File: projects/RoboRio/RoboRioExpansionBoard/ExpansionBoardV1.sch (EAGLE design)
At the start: 36 parts, among them IC1 MCP3008, Q1 5MHz

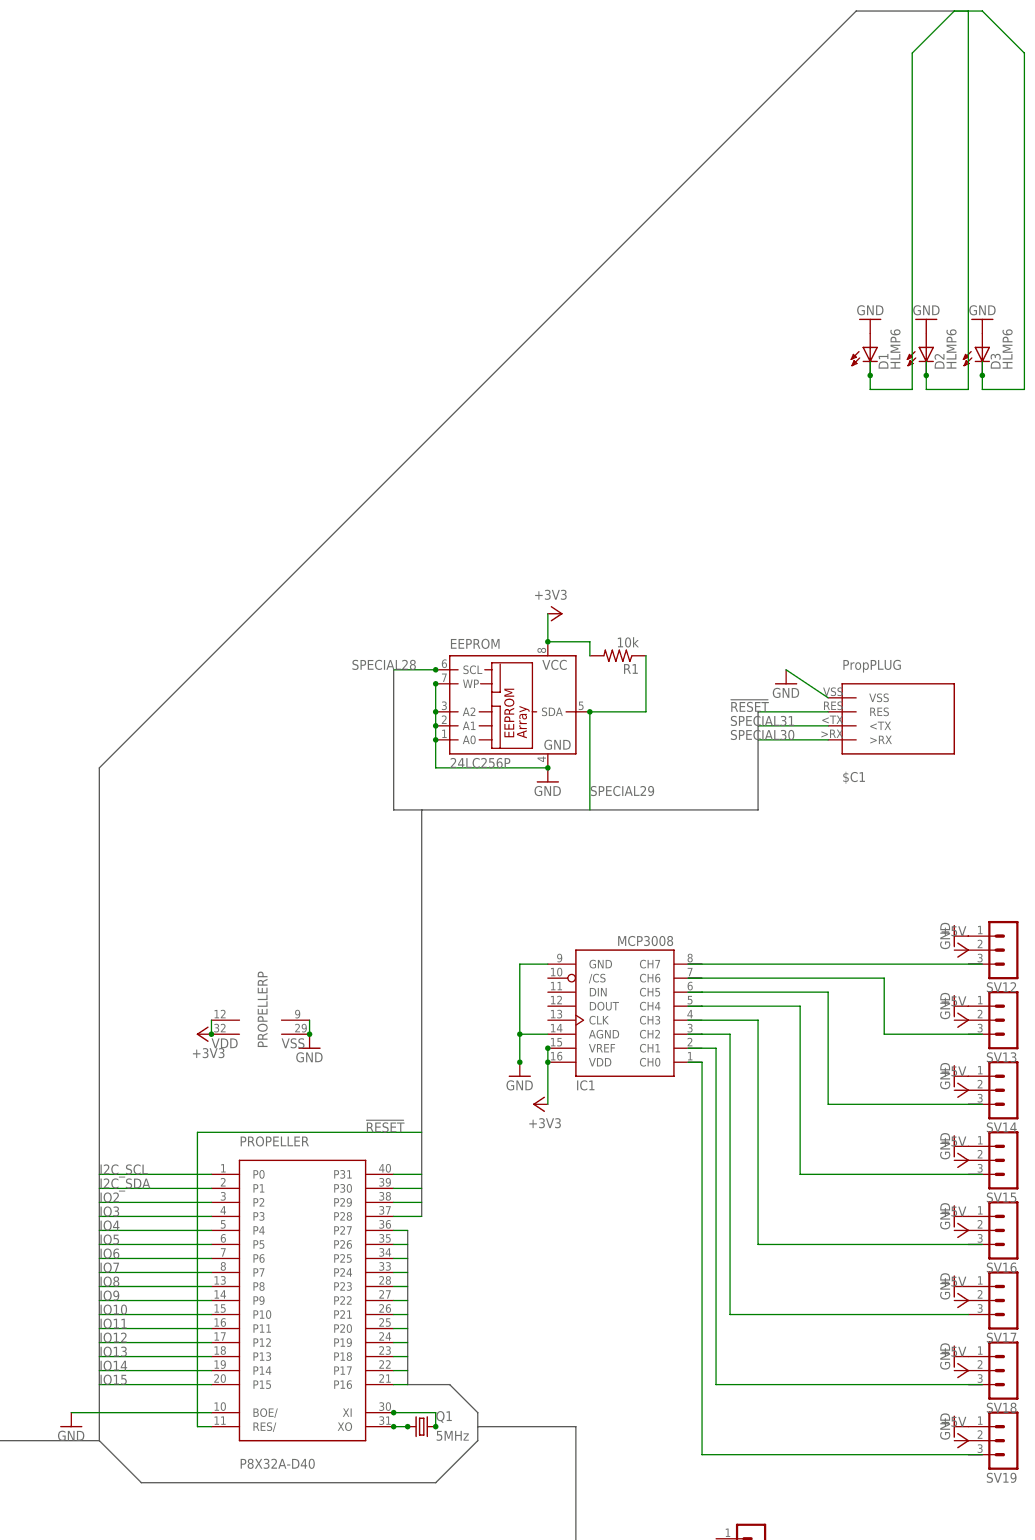
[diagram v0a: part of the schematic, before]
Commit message: RE-Revised LED location
And made them take up significantly less space.
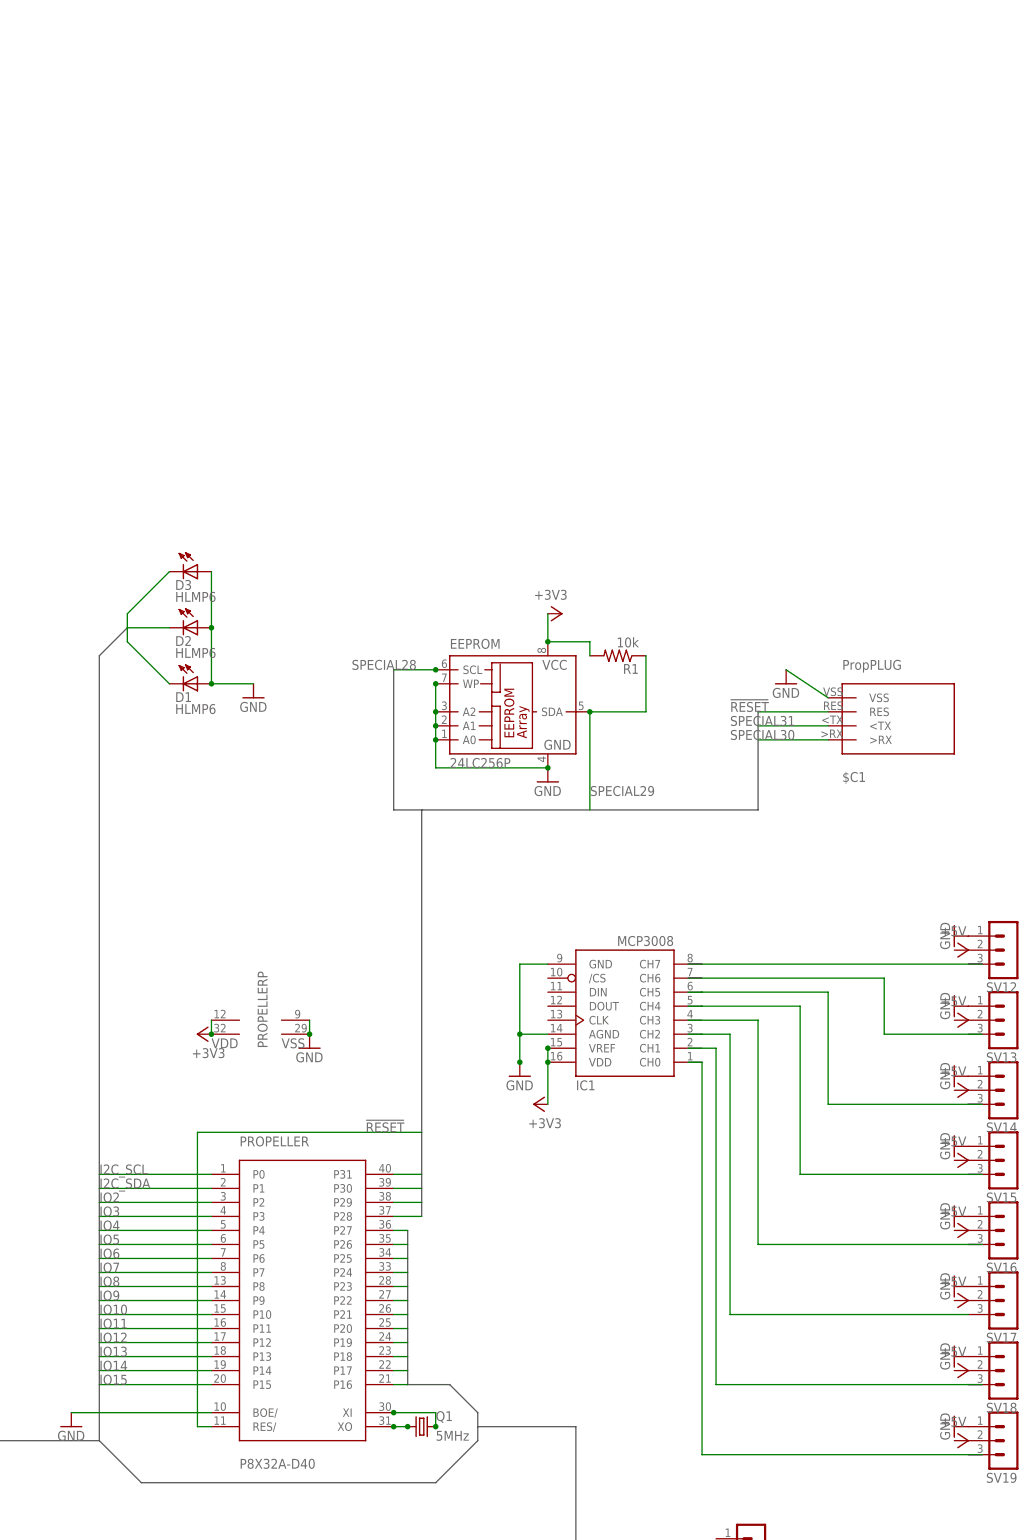
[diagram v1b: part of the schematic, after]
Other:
- moved on the sheet: D1, D2, D3
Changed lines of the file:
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@@
 <part name="D2" library="display-hp" deviceset="HLMP6" device=""/>
 <part name="D3" library="display-hp" deviceset="HLMP6" device=""/>
-<part name="GND8" library="supply1" deviceset="GND" device=""/>
-<part name="GND9" library="supply1" deviceset="GND" device=""/>
 <part name="GND10" library="supply1" deviceset="GND" device=""/>
 <part name="SV12" library="con-lstb" deviceset="MA03-1" device=""/>
@@
 <instance part="GND7" gate="1" x="78.74" y="114.3"/>
 <instance part="+3V5" gate="G$1" x="81.28" y="109.22" rot="R90"/>
-<instance part="D1" gate="A" x="142.24" y="243.84"/>
-<instance part="D2" gate="A" x="152.4" y="243.84"/>
-<instance part="D3" gate="A" x="162.56" y="243.84"/>
-<instance part="GND8" gate="1" x="142.24" y="251.46" rot="R180"/>
-<instance part="GND9" gate="1" x="152.4" y="251.46" rot="R180"/>
-<instance part="GND10" gate="1" x="162.56" y="251.46" rot="R180"/>
+<instance part="D1" gate="A" x="17.78" y="185.42" rot="R270"/>
+<instance part="D2" gate="A" x="17.78" y="195.58" rot="R270"/>
+<instance part="D3" gate="A" x="17.78" y="205.74" rot="R270"/>
+<instance part="GND10" gate="1" x="30.48" y="182.88"/>
 <instance part="SV12" gate="G$1" x="167.64" y="137.16" rot="R180"/>
 <instance part="SV13" gate="G$1" x="167.64" y="124.46" rot="R180"/>
@@
 <wire x1="10.16" y1="40.64" x2="2.54" y2="48.26" width="0.762" layer="92"/>
 <wire x1="2.54" y1="48.26" x2="-63.5" y2="48.26" width="0.762" layer="92"/>
-<wire x1="2.54" y1="48.26" x2="2.54" y2="170.18" width="0.762" layer="92"/>
-<wire x1="2.54" y1="170.18" x2="139.7" y2="307.34" width="0.762" layer="92"/>
-<wire x1="139.7" y1="307.34" x2="160.02" y2="307.34" width="0.762" layer="92"/>
+<wire x1="2.54" y1="48.26" x2="2.54" y2="190.5" width="0.762" layer="92"/>
+<wire x1="2.54" y1="190.5" x2="7.62" y2="195.58" width="0.762" layer="92"/>
 <wire x1="71.12" y1="50.8" x2="88.9" y2="50.8" width="0.762" layer="92"/>
 <wire x1="88.9" y1="50.8" x2="88.9" y2="-50.8" width="0.762" layer="92"/>
@@
 <segment>
 <pinref part="D1" gate="A" pin="A"/>
-<pinref part="GND8" gate="1" pin="GND"/>
-</segment>
-<segment>
+<pinref part="GND10" gate="1" pin="GND"/>
+<wire x1="30.48" y1="185.42" x2="22.86" y2="185.42" width="0.1524" layer="91"/>
+<pinref part="D3" gate="A" pin="A"/>
 <pinref part="D2" gate="A" pin="A"/>
-<pinref part="GND9" gate="1" pin="GND"/>
-</segment>
-<segment>
-<pinref part="D3" gate="A" pin="A"/>
-<pinref part="GND10" gate="1" pin="GND"/>
+<wire x1="22.86" y1="195.58" x2="22.86" y2="205.74" width="0.1524" layer="91"/>
+<wire x1="22.86" y1="195.58" x2="22.86" y2="185.42" width="0.1524" layer="91"/>
+<junction x="22.86" y="185.42"/>
+<junction x="22.86" y="195.58"/>
 </segment>
 <segment>
@@
 </segment>
 <segment>
-<wire x1="162.56" y1="238.76" x2="162.56" y2="241.3" width="0.1524" layer="91"/>
-<wire x1="162.56" y1="241.3" x2="162.56" y2="243.84" width="0.1524" layer="91"/>
-<wire x1="170.18" y1="238.76" x2="162.56" y2="238.76" width="0.1524" layer="91"/>
-<wire x1="170.18" y1="299.72" x2="170.18" y2="238.76" width="0.1524" layer="91"/>
-<wire x1="160.02" y1="307.34" x2="162.56" y2="307.34" width="0.1524" layer="91"/>
-<wire x1="162.56" y1="307.34" x2="170.18" y2="299.72" width="0.1524" layer="91"/>
+<wire x1="7.62" y1="195.58" x2="7.62" y2="198.12" width="0.1524" layer="91"/>
+<wire x1="7.62" y1="198.12" x2="15.24" y2="205.74" width="0.1524" layer="91"/>
 <pinref part="D3" gate="A" pin="K"/>
-<junction x="162.56" y="241.3"/>
 </segment>
 </net>
@@
 </segment>
 <segment>
-<wire x1="160.02" y1="307.34" x2="160.02" y2="238.76" width="0.1524" layer="91"/>
-<wire x1="160.02" y1="238.76" x2="152.4" y2="238.76" width="0.1524" layer="91"/>
-<wire x1="152.4" y1="243.84" x2="152.4" y2="241.3" width="0.1524" layer="91"/>
+<wire x1="7.62" y1="195.58" x2="15.24" y2="195.58" width="0.1524" layer="91"/>
 <pinref part="D2" gate="A" pin="K"/>
-<wire x1="152.4" y1="241.3" x2="152.4" y2="238.76" width="0.1524" layer="91"/>
-<junction x="152.4" y="241.3"/>
 </segment>
 </net>
@@
 </segment>
 <segment>
-<wire x1="149.86" y1="299.72" x2="149.86" y2="238.76" width="0.1524" layer="91"/>
-<wire x1="149.86" y1="299.72" x2="157.48" y2="307.34" width="0.1524" layer="91"/>
-<wire x1="160.02" y1="307.34" x2="157.48" y2="307.34" width="0.1524" layer="91"/>
-<wire x1="142.24" y1="238.76" x2="142.24" y2="241.3" width="0.1524" layer="91"/>
-<wire x1="142.24" y1="241.3" x2="142.24" y2="243.84" width="0.1524" layer="91"/>
-<wire x1="149.86" y1="238.76" x2="142.24" y2="238.76" width="0.1524" layer="91"/>
+<wire x1="15.24" y1="185.42" x2="7.62" y2="193.04" width="0.1524" layer="91"/>
+<wire x1="7.62" y1="195.58" x2="7.62" y2="193.04" width="0.1524" layer="91"/>
 <pinref part="D1" gate="A" pin="K"/>
-<junction x="142.24" y="241.3"/>
-</segment>
-</net>
+</segment>
+</net>

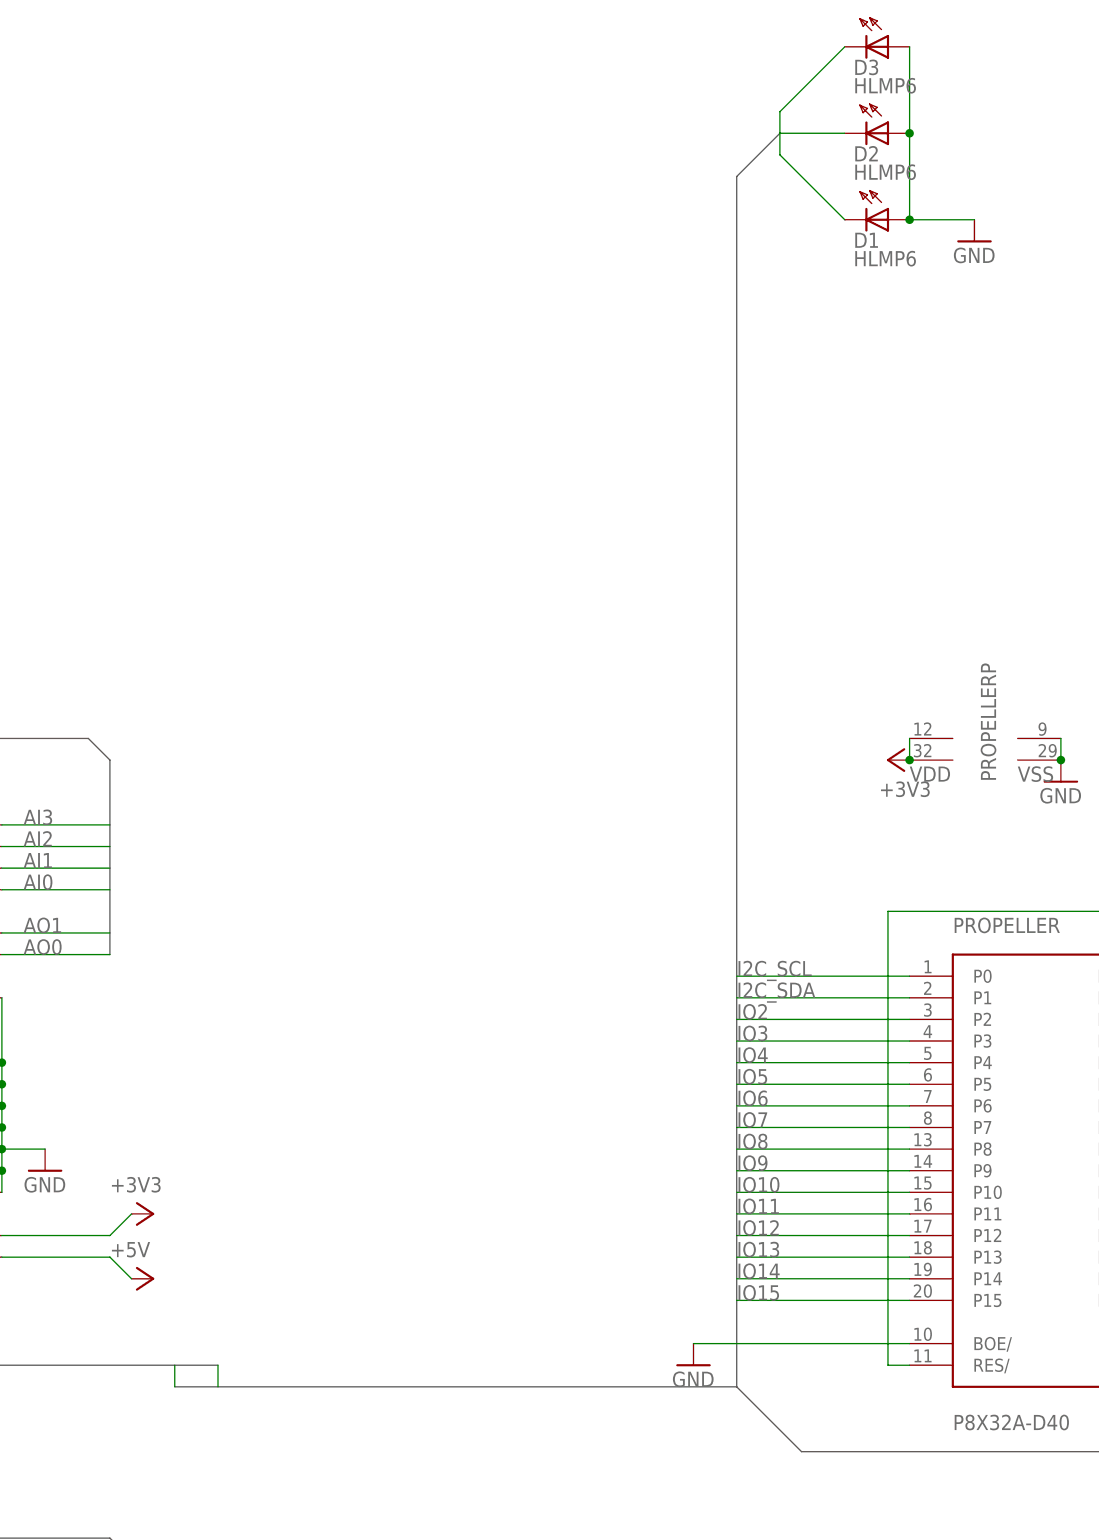
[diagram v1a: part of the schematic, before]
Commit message: Switched to SPI for the connection, adjusted LEDs
LEDs are now on pins 4..6, and named according to color
SPI is for the RoboRIO connection
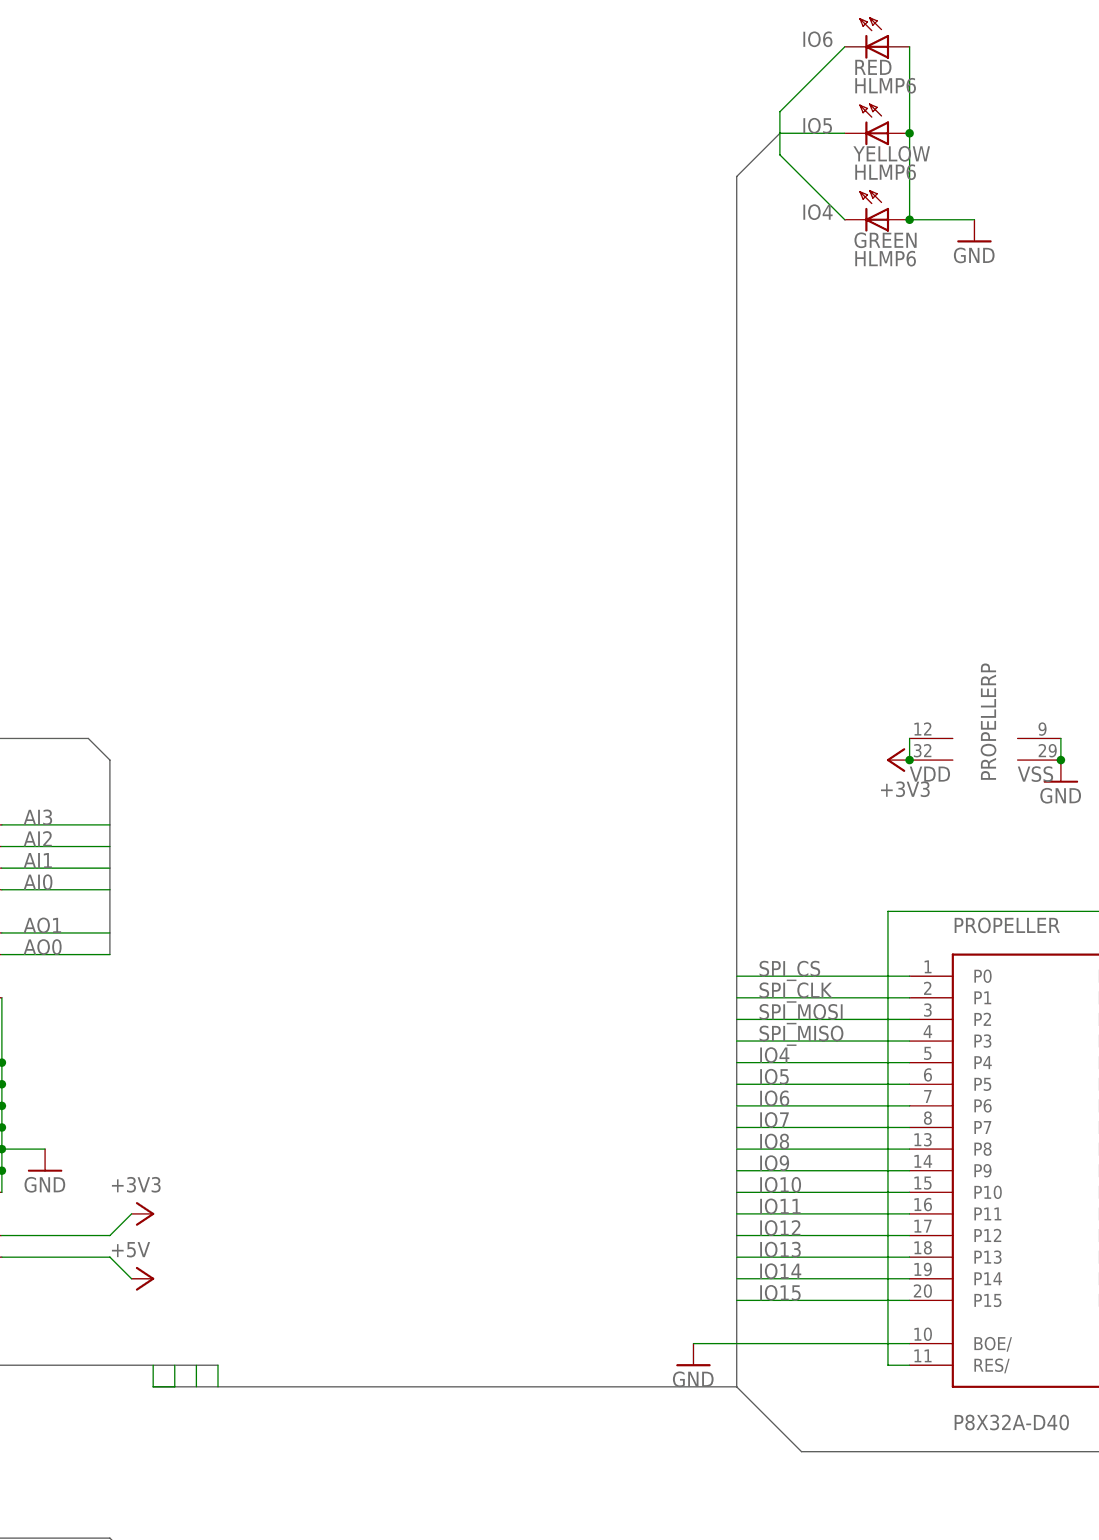
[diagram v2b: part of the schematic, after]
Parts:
- renumbered D1 to GREEN, D2 to YELLOW, D3 to RED
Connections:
- removed net IO2: PROPELLERP8X32A-D40.P2, RED.K
- removed net IO3: PROPELLERP8X32A-D40.P3, YELLOW.K
- net I2C_SCL: no longer PROPELLERP8X32A-D40.P0
- net I2C_SDA: no longer PROPELLERP8X32A-D40.P1
- net IO5: now also YELLOW.K
- net IO6: now also RED.K
- net SPI_CLK: now also PROPELLERP8X32A-D40.P1
- net SPI_CS: now also PROPELLERP8X32A-D40.P0
- net SPI_MISO: now also PROPELLERP8X32A-D40.P3
- net SPI_MOSI: now also PROPELLERP8X32A-D40.P2

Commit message: Renamed connectors, added level shifter
and removed a repeated RR gpio pass-thorough
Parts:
- removed SV1: (no value), con-lstb:MA03-1
- added IC2: 40109, 40xx-2:40109
- added NEOPIXEL: (no value), con-lstb:MA03-1
- renumbered SV10 to RRDIO12, SV11 to RRDIO13, SV12 to ADC7, SV13 to ADC6, SV14 to ADC5, SV15 to ADC4, SV16 to ADC3, SV17 to ADC2, SV18 to ADC1, SV19 to ADC0, SV2 to RRDIO0, SV3 to RRDIO1, SV4 to RRDIO2, SV5 to RRDIO3, SV6 to RRDIO8, SV7 to RRDIO9, SV8 to RRDIO10, SV9 to RRDIO11
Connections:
- new net N$11: IC2A.OUT, NEOPIXEL.3
- net +3V3: now also IC2P.VCC
- net +5V: now also IC2P.VDD; no longer SV1.2
- net DIO0: now also RRDIO0.1; no longer SV1.1
- net DIO1: now also RRDIO1.1; no longer RRDIO0.1
- net DIO10: no longer RRDIO9.1
- net DIO2: now also RRDIO2.1; no longer RRDIO1.1
- net DIO3: now also RRDIO3.1; no longer RRDIO2.1
- net DIO8: now also RRDIO8.1; no longer RRDIO3.1
- net DIO9: now also RRDIO9.1; no longer RRDIO8.1
- net GND: now also IC2P.VSS, NEOPIXEL.1; no longer SV1.3
- net IO7: now also IC2A.IN

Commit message: Connected level shifter
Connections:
- net +3V3: now also IC2A.ENABLE; no longer IC1.VREF
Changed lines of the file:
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@@
 <part name="GND9" library="supply1" deviceset="GND" device=""/>
 <part name="+3V6" library="supply1" deviceset="+3V3" device=""/>
+<part name="+3V7" library="supply1" deviceset="+3V3" device=""/>
 </parts>
 <sheets>
@@
 <instance part="+3V3" gate="G$1" x="-68.58" y="-22.86" rot="R270"/>
 <instance part="P+2" gate="1" x="-68.58" y="-30.48" rot="R270"/>
-<instance part="GND6" gate="1" x="-2.54" y="50.8"/>
+<instance part="GND6" gate="1" x="12.7" y="50.8"/>
 <instance part="+3V4" gate="G$1" x="20.32" y="121.92" rot="R90"/>
 <instance part="PROPELLER" gate="P" x="33.02" y="119.38"/>
@@
 <instance part="GND9" gate="1" x="48.26" y="27.94"/>
 <instance part="+3V6" gate="G$1" x="33.02" y="7.62" rot="R270"/>
+<instance part="+3V7" gate="G$1" x="12.7" y="20.32" rot="R90"/>
 </instances>
 <busses>
@@
 <pinref part="PROPELLER" gate="P8X32A-D40" pin="BOE/"/>
 <pinref part="GND6" gate="1" pin="GND"/>
-<wire x1="22.86" y1="53.34" x2="-2.54" y2="53.34" width="0.1524" layer="91"/>
+<wire x1="22.86" y1="53.34" x2="12.7" y2="53.34" width="0.1524" layer="91"/>
 </segment>
 <segment>
@@
 <pinref part="IC1" gate="G$1" pin="VDD"/>
 <wire x1="83.82" y1="109.22" x2="83.82" y2="116.84" width="0.1524" layer="91"/>
-<wire x1="83.82" y1="119.38" x2="83.82" y2="116.84" width="0.1524" layer="91"/>
-<pinref part="IC1" gate="G$1" pin="VREF"/>
-<junction x="83.82" y="116.84"/>
-<junction x="83.82" y="119.38"/>
 </segment>
 <segment>
@@
 <pinref part="+3V6" gate="G$1" pin="+3V3"/>
 </segment>
-</net>
+<segment>
+<pinref part="IC2" gate="A" pin="ENABLE"/>
+<pinref part="+3V7" gate="G$1" pin="+3V3"/>
+</segment>
+</net>
